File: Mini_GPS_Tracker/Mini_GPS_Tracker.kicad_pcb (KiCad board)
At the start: 2 copper layers, 32 parts, among them J1 USB_C_Receptacle, J2 5-1814400-1, J3 XT60-M, SW1 SW_Push, U1 CH340E, U2 XBee_SMT, U3 MAX-8Q, U4 LD1117S33TR_SOT223, U5 MS5611-01BA, Y1 Crystal

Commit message: updates to routing
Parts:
- added FB1: Ferrite_Bead_Small, Capacitor_SMD:C_0805_2012Metric_Pad1.15x1.40mm_HandSolder, F.Cu at (125.7, 88.9)
- added FB2: Ferrite_Bead_Small, Capacitor_SMD:C_0805_2012Metric_Pad1.15x1.40mm_HandSolder, F.Cu at (126.0, 85.1)
- moved U4 130.6 mm to (252.7, 97.8)
- moved C2 55.3 mm to (185.4, 105.4)
- moved R2 44.4 mm to (178.2, 108.4)
- moved R3 44.4 mm to (178.2, 111.4)
- moved R4 44.4 mm to (183.0, 108.4)
- moved C3 44.4 mm to (173.5, 110.8)
- moved C5 44.4 mm to (174.8, 105.5)
- moved C7 44.4 mm to (179.6, 105.5)
- moved Y1 44.4 mm to (182.8, 111.3)
- moved C13 44.4 mm to (171.6, 110.7)
- moved C12 16.0 mm to (171.4, 86.4)
- moved J1 12.8 mm to (97.8, 115.6)
- moved U1 10.9 mm to (97.8, 104.1)
- moved U3 9.46 mm to (137.2, 87.6)
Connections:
- AE1 pad 1: Net-(AE1-Pad1) -> GND
- MD1 pad 4: Net-(MD1-Pad4) -> GPS_RX
- MD1 pad 56: Net-(MD1-Pad56) -> GPS_TX
- U3 pad 11: Net-(AE1-Pad1) -> Net-(AE1-Pad3)

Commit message: worked on routing
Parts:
- moved AE1 126.0 mm to (132.1, 20.3)
- moved D1 101.4 mm to (153.7, 148.6), turned to 90 degrees
- moved U5 99.6 mm to (222.2, 116.8)
- moved C10 94.1 mm to (97.8, 35.6)
- moved D2 90.7 mm to (149.9, 148.6), turned to 90 degrees
- moved R5 90.7 mm to (149.9, 144.8), turned to 90 degrees
- moved J2 78.9 mm to (186.7, 33.0)
- moved U1 74.6 mm to (152.4, 154.9), turned to 180 degrees
- moved C6 72.3 mm to (171.4, 113.0)
- moved FB1 71.6 mm to (90.4, 26.7), turned to 0 degrees
- moved FB2 70.7 mm to (90.2, 24.1), turned to 0 degrees
- moved U3 69.0 mm to (102.2, 28.2)
- moved J3 65.1 mm to (203.2, 83.8)
- moved C5 58.9 mm to (149.9, 158.8), turned to 90 degrees
- moved SW1 58.4 mm to (168.9, 104.1), turned to 90 degrees
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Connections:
- MD1 pad 12: Net-(MD1-Pad12) -> Pressure_SCL
- MD1 pad 23: Net-(MD1-Pad23) -> Pressure_SDA

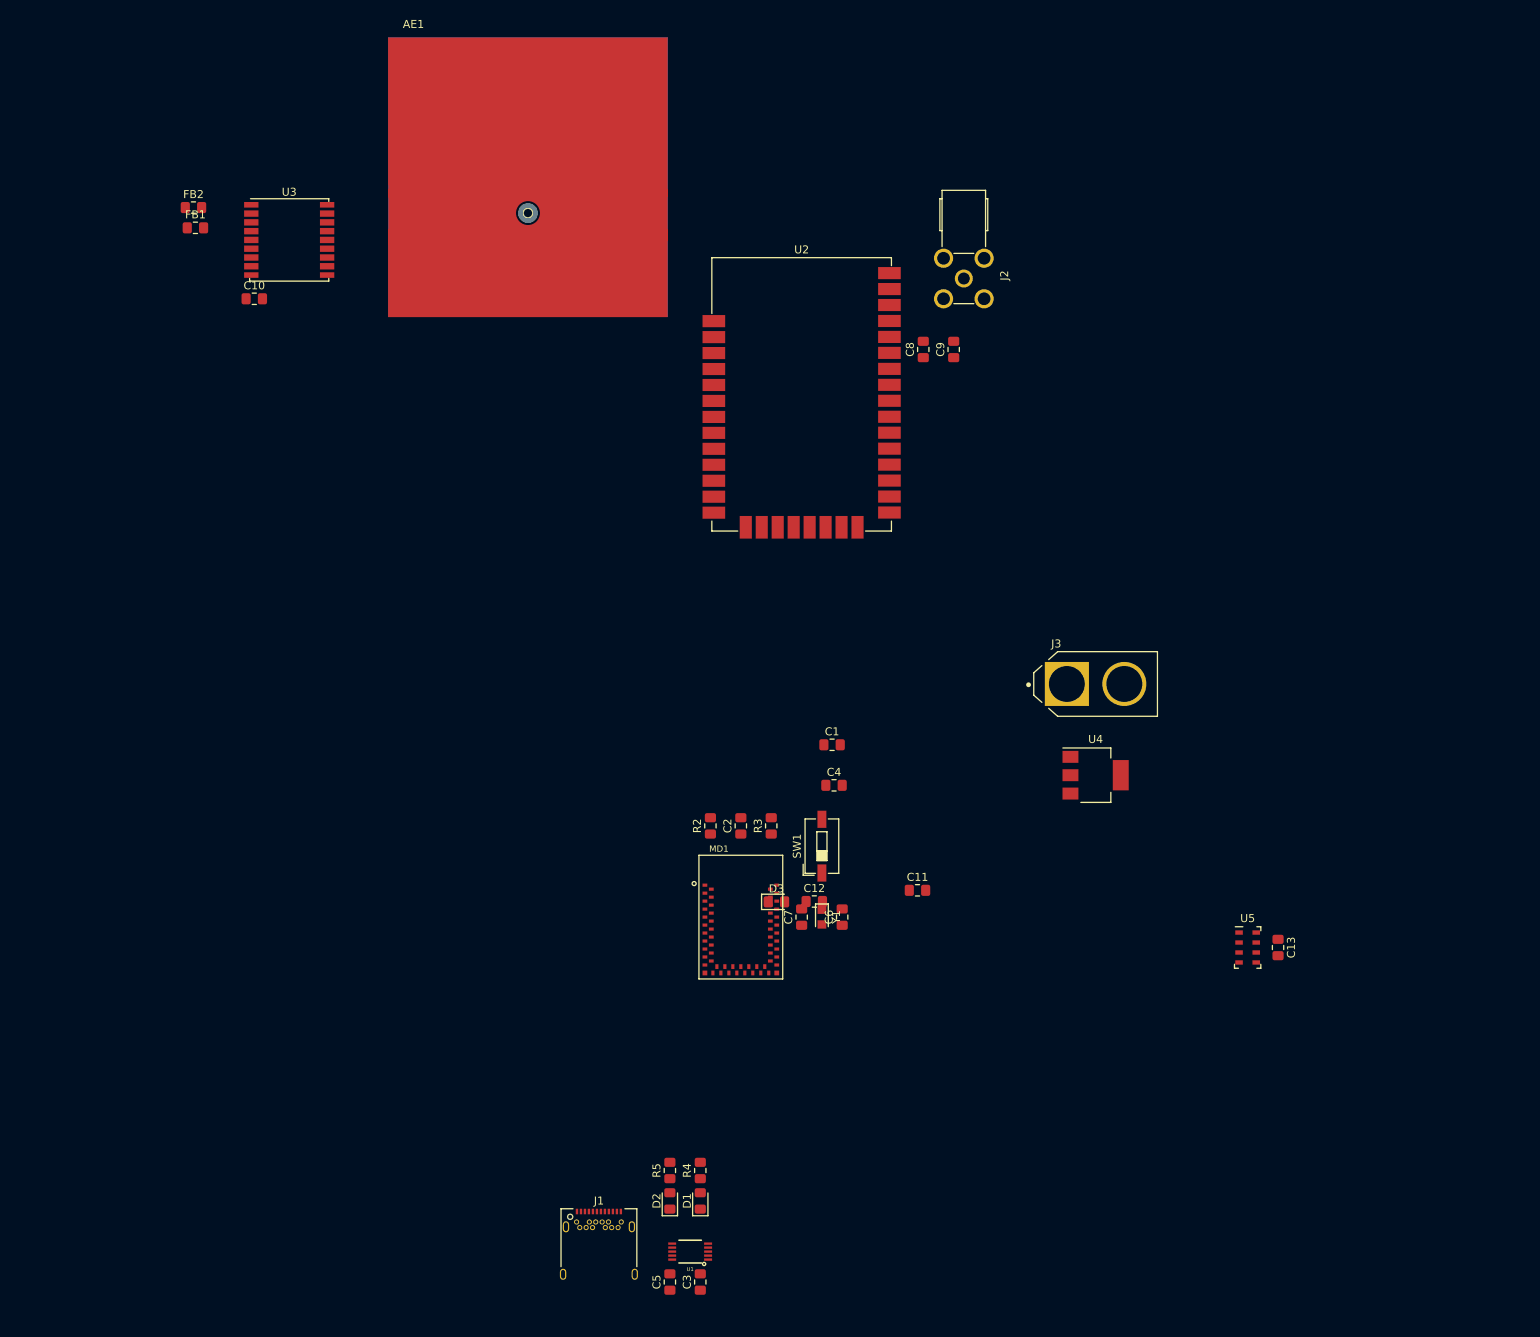
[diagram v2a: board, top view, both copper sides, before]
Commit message: updated antenna;
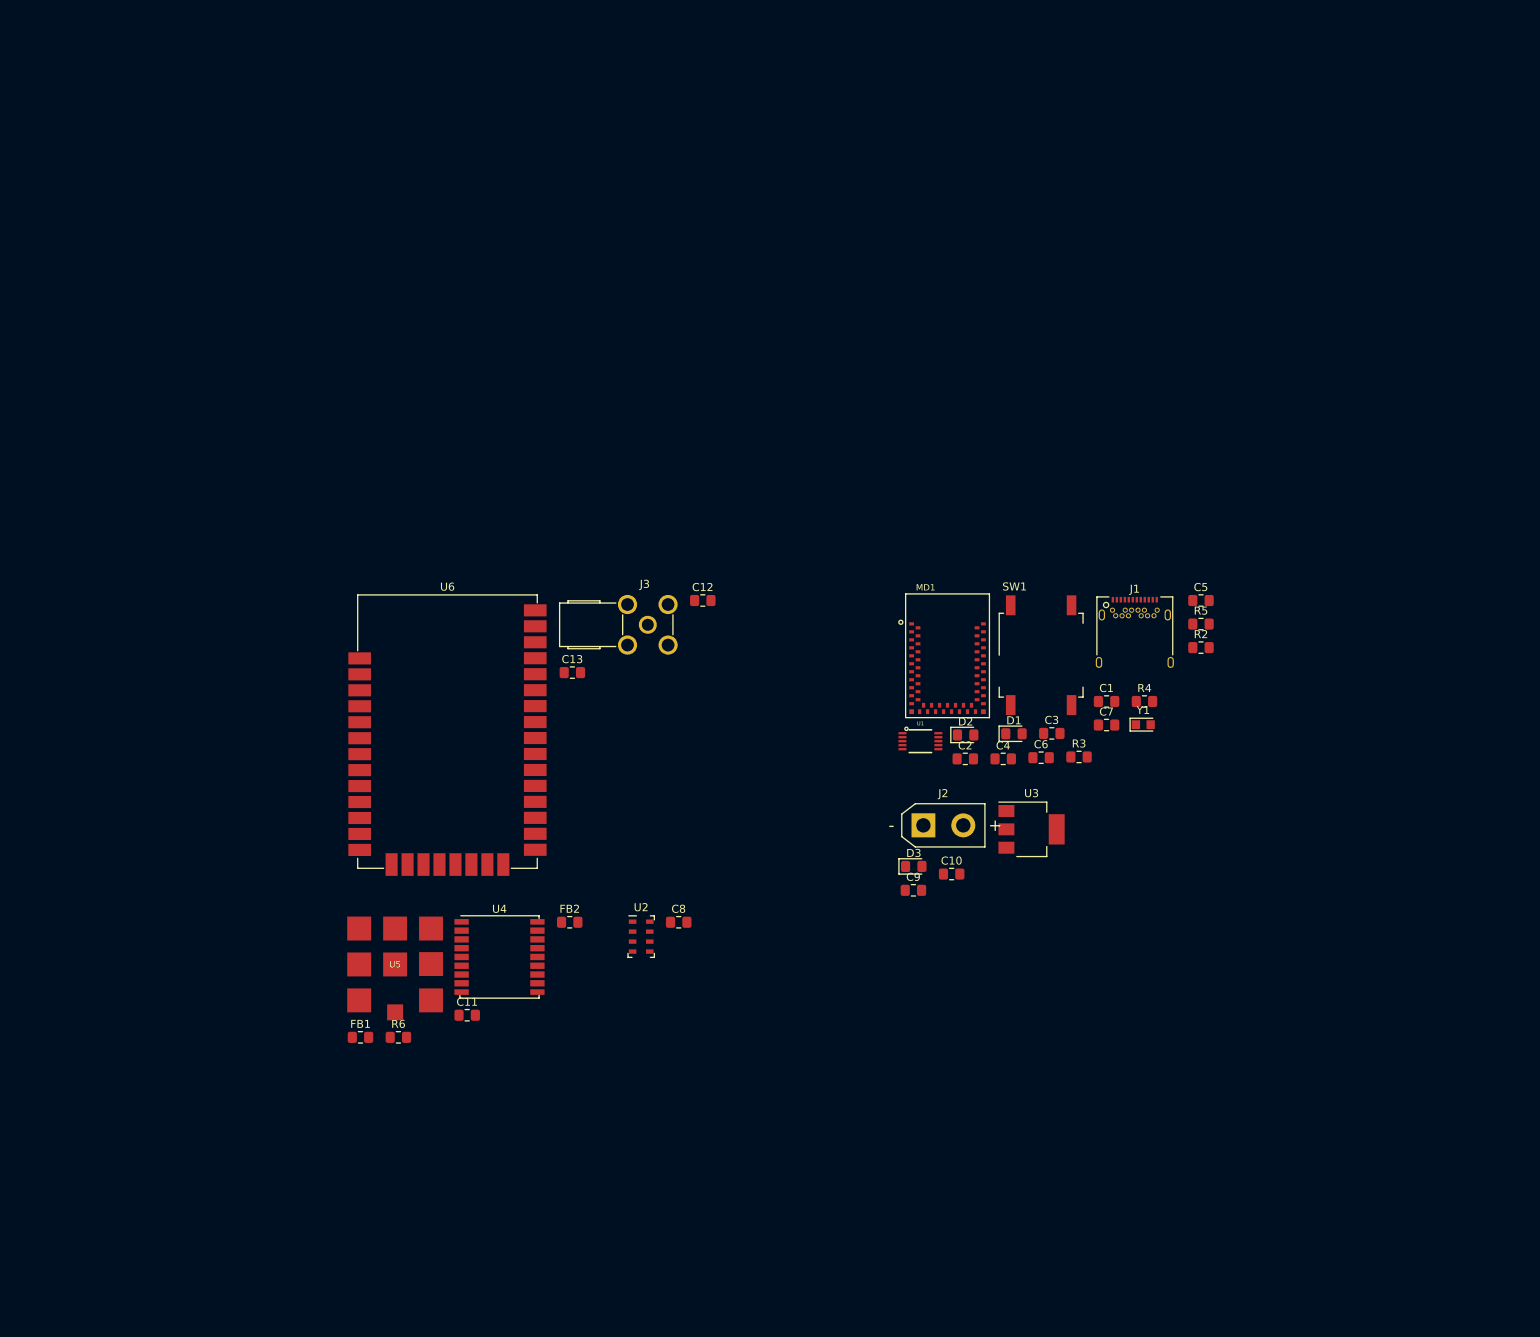
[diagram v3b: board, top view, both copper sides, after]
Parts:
- removed AE1: CGGBP.35.6.A.02, Sparkfun-Artemis:XCVR_CGGBP.35.6.A.02
- added R6: R, Resistor_SMD:R_0805_2012Metric_Pad1.15x1.40mm_HandSolder, F.Cu at (115.8, 128.1)
- added U6: XBee_SMT, RF_Module:Digi_XBee_SMT, F.Cu at (122.0, 90.5)
- C10: value 0.1uF -> 100nF
- C11: value 100nF -> 0.1uF
- C12: value 100nF -> 100pF
- C13: value 100nF -> 1.0uF
- C8: value 100pF -> 100nF
- C9: value 1.0uF -> 100nF
- J2: value 5-1814400-1 -> Screw_Terminal_01x02; footprint Sparkfun-Artemis:CONN_5-1814400-1 -> Connector_AMASS:AMASS_XT30UPB-F_1x02_P5.0mm_Vertical
- J3: value XT60-M -> 5-1814400-1; footprint Sparkfun-Artemis:AMASS_XT60-M -> Sparkfun-Artemis:CONN_5-1814400-1
- SW1: footprint Button_Switch_SMD:SW_DIP_SPSTx01_Slide_6.7x4.1mm_W6.73mm_P2.54mm_LowProfile_JPin -> Button_Switch_SMD:SW_MEC_5GSH9
- U2: value XBee_SMT -> MS5611-01BA; footprint RF_Module:Digi_XBee_SMT -> Package_LGA:LGA-8_3x5mm_P1.25mm
- U3: value MAX-8Q -> LD1117S33TR_SOT223; footprint RF_GPS:ublox_MAX -> Package_TO_SOT_SMD:SOT-223-3_TabPin2
- U4: value LD1117S33TR_SOT223 -> MAX-8Q; footprint Package_TO_SOT_SMD:SOT-223-3_TabPin2 -> RF_GPS:ublox_MAX
- U5: value MS5611-01BA -> SGGP.12.4.A.02; footprint Package_LGA:LGA-8_3x5mm_P1.25mm -> RF_Antenna:SGGP.12.4.A.02
- moved U3 118.8 mm to (195.2, 102.0)
- moved C10 113.3 mm to (185.2, 107.6)
- moved C5 108.3 mm to (216.4, 73.4), turned to 0 degrees
- moved U5 106.8 mm to (115.4, 119.0)
- moved FB1 103.5 mm to (111.1, 128.1)
- moved J1 101.9 mm to (208.1, 78.3)
- moved FB2 101.2 mm to (137.3, 113.7)
- moved R5 95.5 mm to (216.4, 76.3), turned to 0 degrees
- moved C13 94.9 mm to (137.6, 82.4), turned to 0 degrees
- moved C3 81.6 mm to (197.7, 90.0), turned to 0 degrees
- moved R4 80.9 mm to (209.3, 86.0), turned to 0 degrees
- moved U4 78.1 mm to (128.5, 118.0)
- moved C8 78.0 mm to (151.0, 113.7), turned to 0 degrees
- moved D1 70.5 mm to (193.0, 90.1), turned to 0 degrees
- moved U2 70.2 mm to (146.3, 115.5)
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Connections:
- C11 pad 1: Net-(C11-Pad1) -> +3V3
- C8 pad 1: Net-(C8-Pad1) -> +3V3
- C9 pad 1: +3V3 -> Net-(C9-Pad1)
- D3 pad 1: Net-(C12-Pad1) -> Net-(D3-Pad1)
- D3 pad 2: +3V3 -> Net-(C9-Pad1)
- J2 pad 1: Net-(J2-Pad1) -> GND
- J2 pad 2: Net-(J2-Pad1) -> Net-(D3-Pad1)
- J3 pad 1: GND -> Net-(J3-Pad1)
- J3 pad 2: Net-(C11-Pad1) -> Net-(J3-Pad1)
- MD1 pad 17: TRANS_TX -> TRANS_RX
- MD1 pad 18: TRANS_RX -> TRANS_TX
- MD1 pad 4: GPS_RX -> GPS_TX
- MD1 pad 48: TXO -> RXI
- MD1 pad 49: RX0 -> TXO
- MD1 pad 56: GPS_TX -> GPS_RX
- U2 pad 1: GND -> +3V3
- U2 pad 2: Net-(C8-Pad1) -> +3V3
- U2 pad 3: TRANS_TX -> GND
- U2 pad 4: TRANS_RX -> Net-(U2-Pad4)
- U2 pad 5: Net-(U2-Pad5) -> Net-(U2-Pad4)
- U2 pad 7: Net-(U2-Pad7) -> Pressure_SDA
- U2 pad 8: Net-(U2-Pad8) -> Pressure_SCL
- U3 pad 2: Net-(FB2-Pad1) -> +3V3
- U3 pad 3: Net-(FB1-Pad1) -> Net-(C9-Pad1)
- U4 pad 2: Net-(C12-Pad1) -> Net-(FB2-Pad1)
- U4 pad 3: Net-(C11-Pad1) -> Net-(FB1-Pad1)

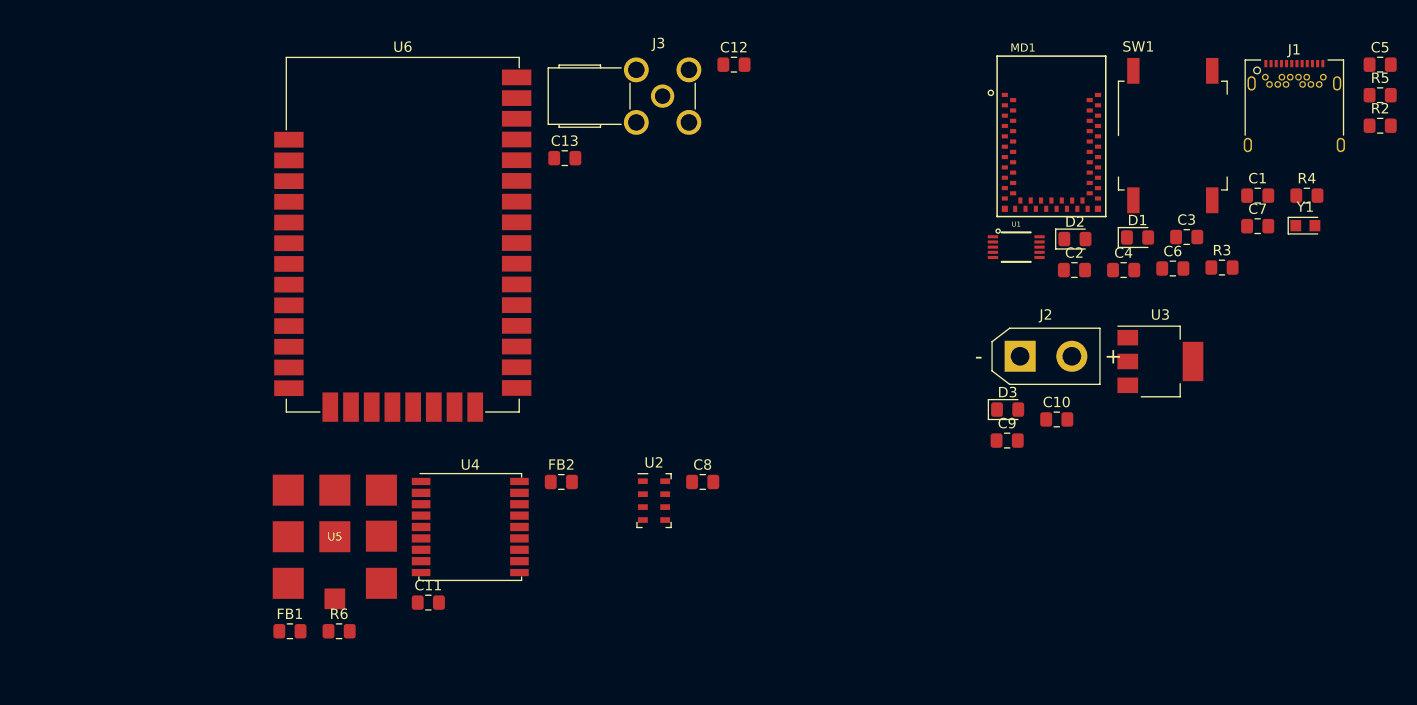
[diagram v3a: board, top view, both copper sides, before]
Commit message: added 9dof
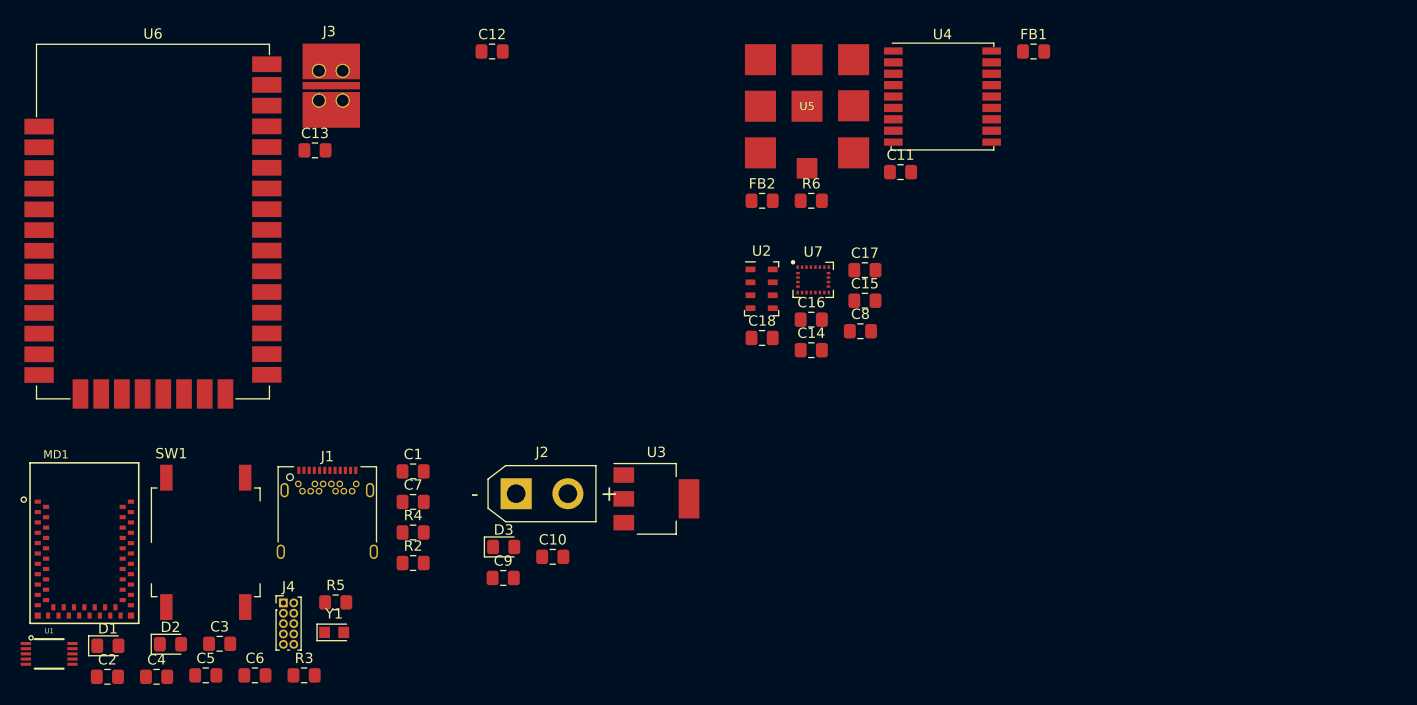
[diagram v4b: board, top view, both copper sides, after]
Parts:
- added C14: 10uF, Capacitor_SMD:C_0805_2012Metric_Pad1.15x1.40mm_HandSolder, F.Cu at (161.5, 100.9)
- added C15: 0.1uF, Capacitor_SMD:C_0805_2012Metric_Pad1.15x1.40mm_HandSolder, F.Cu at (166.6, 96.2)
- added C16: 0.1uF, Capacitor_SMD:C_0805_2012Metric_Pad1.15x1.40mm_HandSolder, F.Cu at (161.5, 98.0)
- added C17: 10nF, Capacitor_SMD:C_0805_2012Metric_Pad1.15x1.40mm_HandSolder, F.Cu at (166.6, 93.2)
- added C18: 0.1uF, Capacitor_SMD:C_0805_2012Metric_Pad1.15x1.40mm_HandSolder, F.Cu at (156.7, 99.8)
- added J4: Conn_ARM_JTAG_SWD_10, Connector_PinHeader_1.00mm:PinHeader_2x05_P1.00mm_Vertical, F.Cu at (110.5, 125.4)
- added U7: LSM9DS1, Package_LGA:LGA-24L_3x3.5mm_P0.43mm, F.Cu at (161.6, 94.2)
- J3: value 5-1814400-1 -> 901-10512-1; footprint Sparkfun-Artemis:CONN_5-1814400-1 -> Sparkfun-Artemis:AMPHENOL_901-10512-1
- moved C5 127.9 mm to (103.0, 132.4)
- moved R5 112.2 mm to (115.5, 125.3)
- moved D1 107.0 mm to (93.5, 129.5)
- moved R2 102.5 mm to (123.0, 121.5)
- moved Y1 101.7 mm to (115.4, 128.2)
- moved J1 101.3 mm to (114.7, 117.6)
- moved C2 101.3 mm to (93.5, 132.5)
- moved C3 101.3 mm to (104.3, 129.3)
- moved C4 101.3 mm to (98.2, 132.5)
- moved MD1 101.3 mm to (91.2, 119.6)
- moved SW1 101.3 mm to (103.0, 119.5)
- moved U1 101.3 mm to (87.8, 130.3)
- moved R3 97.0 mm to (112.5, 132.4)
- moved C6 97.0 mm to (107.7, 132.4)
- moved D2 95.7 mm to (99.6, 129.4)
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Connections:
- C1 pad 2: DTR -> RTS
- C2 pad 2: DTR -> RTS
- MD1 pad 10: Net-(MD1-Pad10) -> SWDCK
- MD1 pad 2: Net-(MD1-Pad2) -> SWDIO
- MD1 pad 33: Net-(MD1-Pad33) -> A1

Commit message: schamatics finalized
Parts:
- added C19: CAP, Capacitor_SMD:C_0805_2012Metric_Pad1.15x1.40mm_HandSolder, F.Cu at (150.0, 100.7)
- added D4: LED, LED_SMD:LED_0805_2012Metric_Pad1.15x1.40mm_HandSolder, F.Cu at (152.5, 124.8)
- added FL1: SAFFA1G58KA0F0A, Filter:Filter_1411-5_1.4x1.1mm, F.Cu at (157.6, 100.7)
- added H1: MountingHole_Pad, MountingHole:MountingHole_3.2mm_M3, F.Cu at (181.6, 135.9)
- added H2: MountingHole_Pad, MountingHole:MountingHole_3.2mm_M3, F.Cu at (181.6, 44.5)
- added H3: MountingHole_Pad, MountingHole:MountingHole_3.2mm_M3, F.Cu at (151.1, 44.5)
- added H4: MountingHole_Pad, MountingHole:MountingHole_3.2mm_M3, F.Cu at (151.1, 135.9)
- added L1: INDUCTOR, Inductor_SMD:L_0805_2012Metric_Pad1.15x1.40mm_HandSolder, F.Cu at (153.9, 100.7)
- added R1: 10k, Resistor_SMD:R_0805_2012Metric_Pad1.15x1.40mm_HandSolder, F.Cu at (174.0, 123.2)
- added SW2: MLL1200S, SW_MLL1200S, F.Cu at (182.9, 125.7)
- added U8: W25Q128JVS, Package_SO:SOIC-8_5.23x5.23mm_P1.27mm, F.Cu at (181.9, 89.7)
- added U9: MAX2686, Package_BGA:WLP-4_0.86x0.86mm_P0.4mm, F.Cu at (149.5, 103.5)
- C10: value 100nF -> 10uF
- R3: value 220K -> 3k
- SW1: footprint Button_Switch_SMD:SW_MEC_5GSH9 -> Sparkfun-Artemis:SW_TL1015AF160QG
- moved C4 87.7 mm to (182.8, 109.1), turned to 180 degrees
- moved MD1 81.0 mm to (168.9, 96.6)
- moved U6 76.8 mm to (171.2, 66.3)
- moved SW1 75.3 mm to (177.0, 106.2), turned to 90 degrees
- moved D1 71.8 mm to (164.0, 115.6)
- moved U1 71.2 mm to (158.9, 125.1), turned to 90 degrees
- moved C2 70.8 mm to (158.0, 103.4)
- moved J4 68.7 mm to (167.3, 86.6), turned to 90 degrees
- moved D2 64.8 mm to (164.0, 122.0)
- moved J3 64.6 mm to (171.6, 44.2), turned to 90 degrees
- moved C6 63.5 mm to (166.4, 108.0), turned to 270 degrees
- moved R3 62.9 mm to (174.0, 119.1), turned to 90 degrees
- moved R2 62.4 mm to (182.8, 103.4)
- moved C5 61.4 mm to (163.8, 124.2)
- moved C1 60.0 mm to (182.8, 106.8)
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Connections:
- C2 pad 1: BOOT -> Net-(C2-Pad1)
- C2 pad 2: RTS -> +3V3
- J1 pad S1: Net-(J1-PadS1) -> GND
- J2 pad 2: Net-(D3-Pad1) -> Net-(J2-Pad2)
- J4 pad 10: RESET_2 -> RESET
- J4 pad 8: GND -> Net-(J4-Pad8)
- MD1 pad 11: Net-(MD1-Pad11) -> cs_flash
- MD1 pad 13: Net-(MD1-Pad13) -> clk_flash
- MD1 pad 42: Net-(MD1-Pad42) -> v_measure
- MD1 pad 49: TXO -> TX0
- MD1 pad 50: nReset -> RESET
- MD1 pad 52: Net-(MD1-Pad52) -> 9_SDA
- MD1 pad 53: Net-(MD1-Pad53) -> 9_SCL
- MD1 pad 58: Net-(MD1-Pad58) -> gps_reset
- MD1 pad 6: Net-(MD1-Pad6) -> MISO_Flash
- MD1 pad 7: BOOT -> Net-(MD1-Pad7)
- MD1 pad 8: Net-(MD1-Pad8) -> MOSI_Flash
- R3 pad 1: BOOT -> v_measure
- R6 pad 2: Net-(R6-Pad2) -> Net-(D4-Pad2)
- U4 pad 11: Net-(R6-Pad2) -> Net-(FL1-Pad4)
- U4 pad 4: Net-(U4-Pad4) -> Net-(R6-Pad1)
- U4 pad 9: Net-(U4-Pad9) -> gps_reset
- U5 pad RF: Net-(R6-Pad1) -> Net-(C19-Pad1)
- U7 pad 2: /Sheet5E70BD5D/9_SCL -> 9_SCL
- U7 pad 4: /Sheet5E70BD5D/9_SDA -> 9_SDA
- U7 pad 5: /Sheet5E70BD5D/9_SDO_AG -> +3V3
- U7 pad 6: /Sheet5E70BD5D/9_SDO_M -> +3V3
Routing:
- net Net-(FL1-Pad1): track 0.00 -> 8.88 mm
- net Net-(C19-Pad1): track 0.00 -> 8.74 mm
- net Net-(L1-Pad1): track 0.00 -> 7.28 mm
- net Net-(C19-Pad2): track 0.00 -> 1.89 mm
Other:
- board outline added: 38.1 x 99.1 mm
